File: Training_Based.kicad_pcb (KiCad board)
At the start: 2 copper layers, 210 x 140 mm, 63 parts, among them J1 Conn_01x19, J2 Conn_01x19, J3 Conn_01x19, J4 Conn_01x19, J5 Conn_01x08, J6 Conn_02x02_Row_Letter_Last, J7 Conn_02x02_Row_Letter_Last, J8 Conn_02x02_Row_Letter_Last, K1 FINDER-36.11, K2 FINDER-36.11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

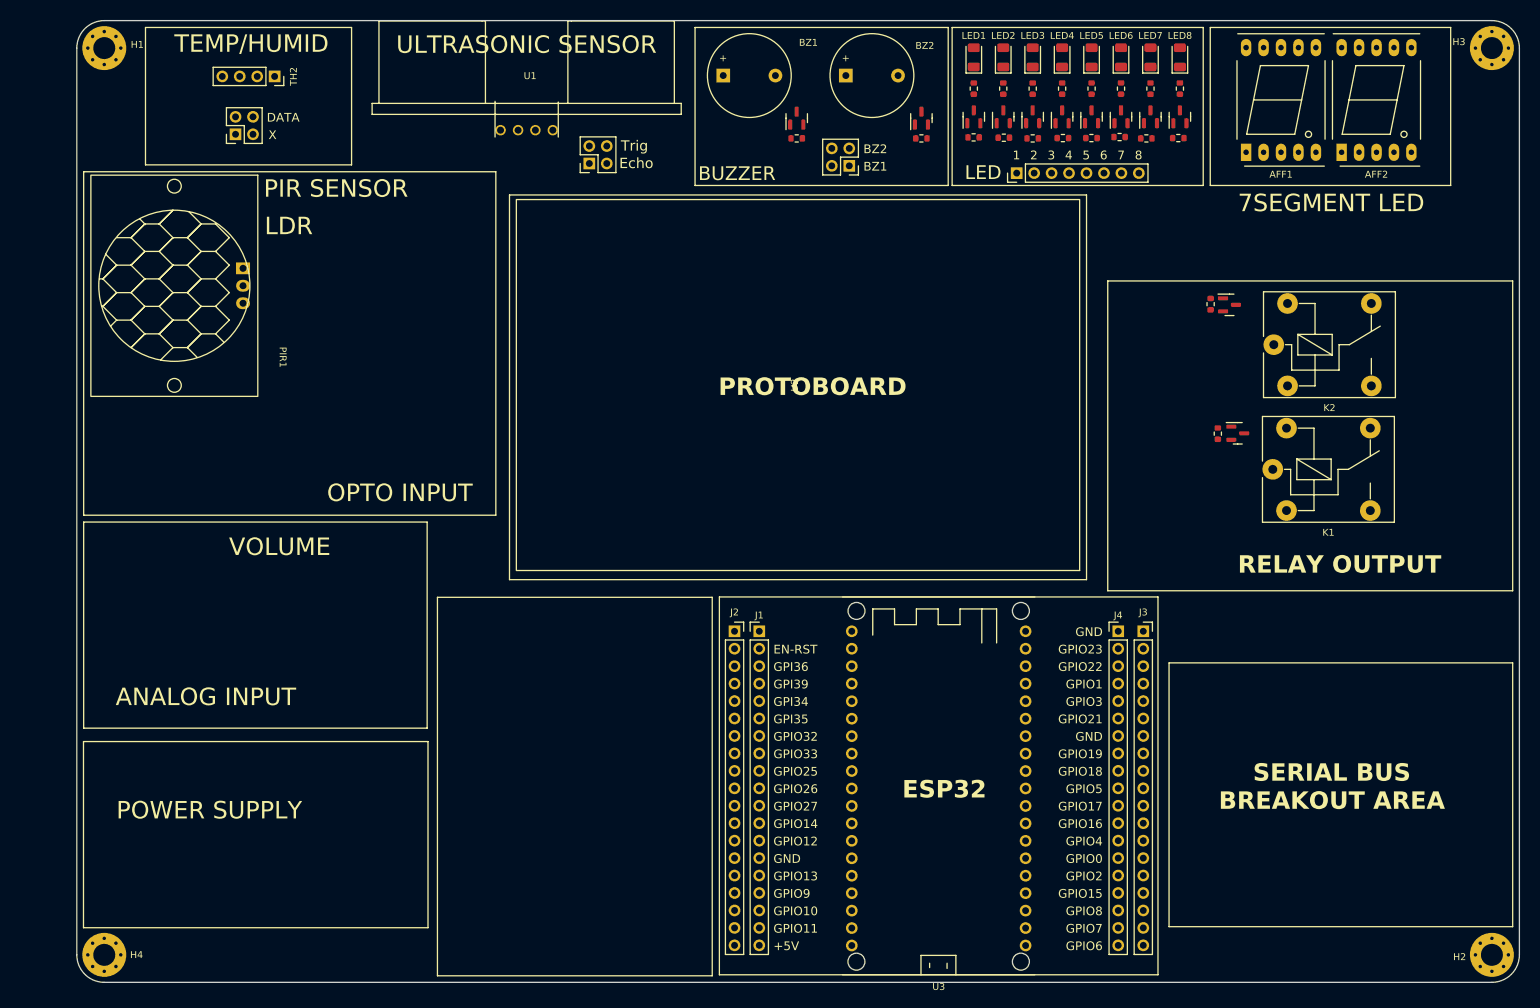
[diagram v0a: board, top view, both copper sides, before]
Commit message: 7 segment and relay
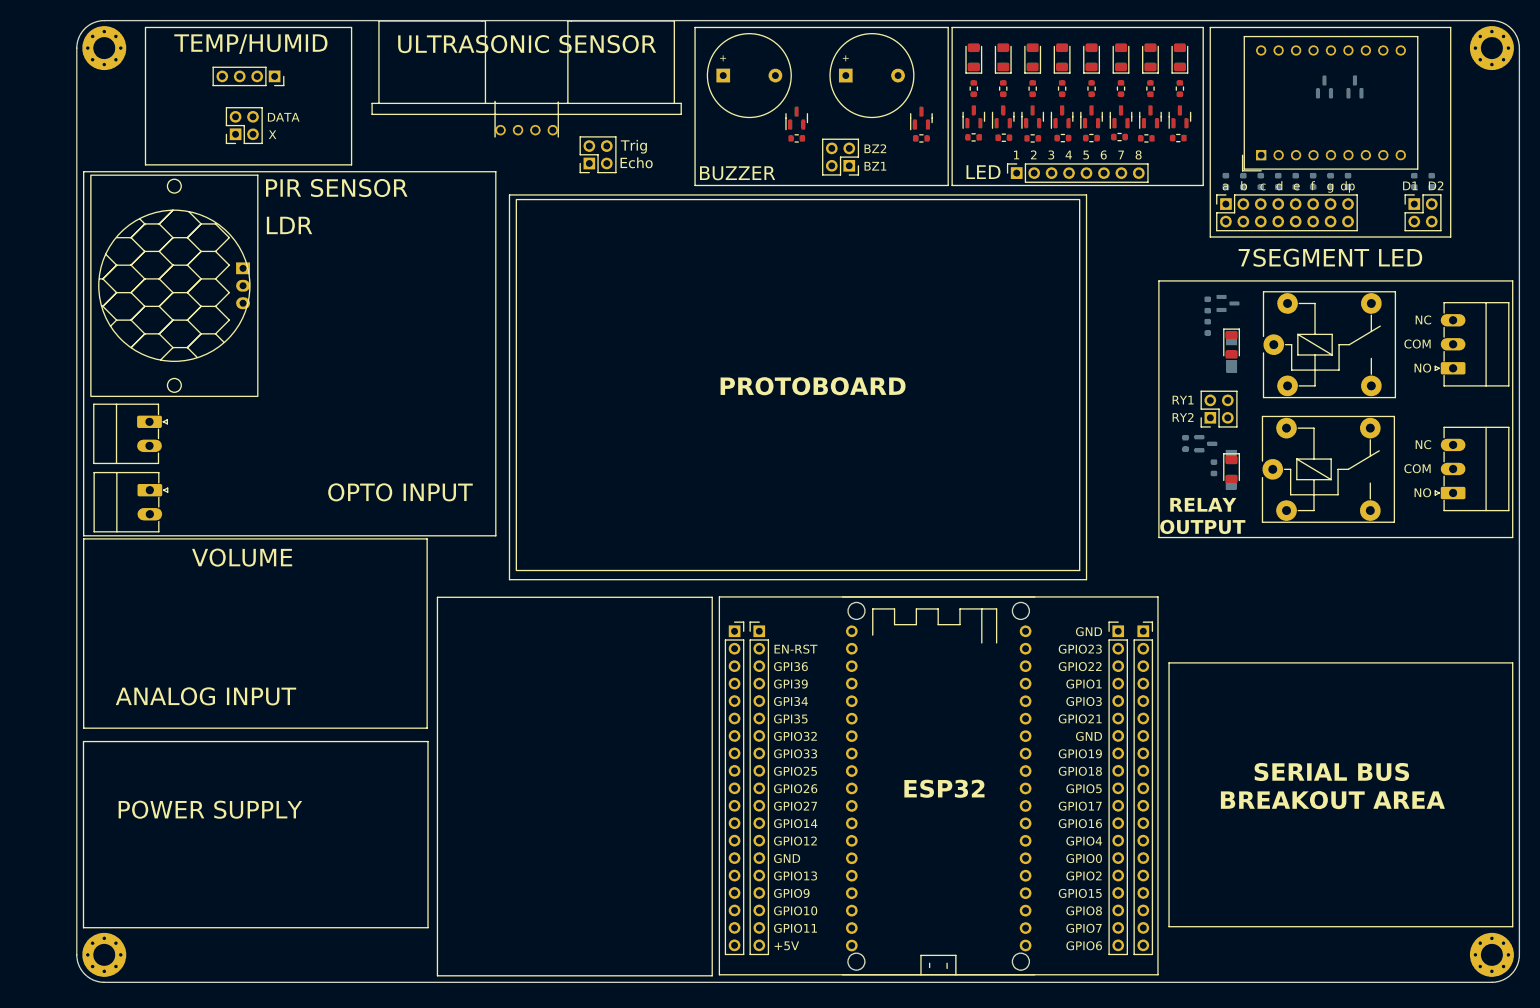
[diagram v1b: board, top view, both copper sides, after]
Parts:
- removed AFF1, AFF2: LTS-6980HR, Display_7Segment:7SegmentLED_LTS6760_LTS6780
- added D1: D, Training_Based:DO-214AC, B.Cu at (188.1, 85.4)
- added D2: D, Training_Based:DO-214AC, B.Cu at (188.1, 68.3)
- added J10: Conn_02x08_Odd_Even, Connector_PinSocket_2.54mm:PinSocket_2x08_P2.54mm_Vertical, F.Cu at (187.3, 46.7)
- added J11: Conn_02x02_Row_Letter_Last, Connector_PinSocket_2.54mm:PinSocket_2x02_P2.54mm_Vertical, F.Cu at (214.7, 46.7)
- added J9: Conn_02x02_Row_Letter_Last, Connector_PinSocket_2.54mm:PinSocket_2x02_P2.54mm_Vertical, F.Cu at (185.0, 77.8)
- added LED10: LED, LED_SMD:LED_1206_3216Metric, F.Cu at (188.1, 67.2)
- added LED9: LED, LED_SMD:LED_1206_3216Metric, F.Cu at (188.1, 85.3)
- added P1: K1, Connector_Phoenix_MC:PhoenixContact_MC_1,5_3-G-3.5_1x03_P3.50mm_Horizontal, F.Cu at (220.3, 88.8)
- added P2: K2, Connector_Phoenix_MC:PhoenixContact_MC_1,5_3-G-3.5_1x03_P3.50mm_Horizontal, F.Cu at (220.3, 70.6)
- added P3: CAN, Connector_Phoenix_MC:PhoenixContact_MC_1,5_2-G-3.5_1x02_P3.50mm_Horizontal, F.Cu at (30.6, 78.4)
- added P4: CAN, Connector_Phoenix_MC:PhoenixContact_MC_1,5_2-G-3.5_1x02_P3.50mm_Horizontal, F.Cu at (30.6, 88.4)
- added Q13: BC817, Package_TO_SOT_SMD:SOT-23, B.Cu at (201.6, 29.6)
- added Q14: BC817, Package_TO_SOT_SMD:SOT-23, B.Cu at (206.1, 29.6)
- added R21: R_Small, Resistor_SMD:R_0603_1608Metric, B.Cu at (214.7, 43.4)
- added R22: R_Small, Resistor_SMD:R_0603_1608Metric, B.Cu at (217.2, 43.4)
- added R23: R_Small, Resistor_SMD:R_0603_1608Metric, B.Cu at (187.3, 43.4)
- added R24: R_Small, Resistor_SMD:R_0603_1608Metric, B.Cu at (189.8, 43.4)
- added R25: R_Small, Resistor_SMD:R_0603_1608Metric, B.Cu at (192.4, 43.4)
- added R26: R_Small, Resistor_SMD:R_0603_1608Metric, B.Cu at (194.9, 43.4)
- added R27: R_Small, Resistor_SMD:R_0603_1608Metric, B.Cu at (197.4, 43.4)
- added R28: R_Small, Resistor_SMD:R_0603_1608Metric, B.Cu at (200.0, 43.4)
- added R29: R_Small, Resistor_SMD:R_0603_1608Metric, B.Cu at (202.5, 43.4)
- added R30: R_Small, Resistor_SMD:R_0603_1608Metric, B.Cu at (205.1, 43.4)
- added R31: R_Small, Resistor_SMD:R_0603_1608Metric, B.Cu at (185.5, 85.1)
- added R32: R_Small, Resistor_SMD:R_0603_1608Metric, B.Cu at (184.6, 64.7)
- added U4: DC56-11SURKWA, Display_7Segment:DA56-11SURKWA, F.Cu at (192.4, 39.6)
- J5: footprint Connector_PinHeader_2.54mm:PinHeader_1x08_P2.54mm_Vertical -> Connector_PinSocket_2.54mm:PinSocket_1x08_P2.54mm_Vertical
- Q11, Q12, R19, R20: moved to B.Cu
- moved R19 4.91 mm to (181.4, 81.5), turned to -90 degrees
- moved Q11 4.89 mm to (184.3, 81.6)
- moved R20 0.44 mm to (184.6, 61.4), turned to -90 degrees
- moved Q12 0.30 mm to (187.6, 61.2)
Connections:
- K1 pad 11: unconnected-(K1-Pad11) -> Net-(P1-Pin_2)
- K1 pad 12: unconnected-(K1-Pad12) -> Net-(P1-Pin_3)
- K1 pad 14: unconnected-(K1-Pad14) -> Net-(P1-Pin_1)
- K2 pad 11: unconnected-(K2-Pad11) -> Net-(P2-Pin_2)
- K2 pad 12: unconnected-(K2-Pad12) -> Net-(P2-Pin_3)
- K2 pad 14: unconnected-(K2-Pad14) -> Net-(P2-Pin_1)
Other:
- board text added: "COM"
- board text added: "D1"
- board text added: "D2"
- board text added: "NC"
- board text added: "NO"
- board text added: "RY1"
- board text added: "RY2"
- board text added: "a"
- board text added: "b"
- board text added: "c"
- board text added: "d"
- board text added: "dp"
- board text added: "e"
- board text added: "f"
- board text added: "g"

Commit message: opto isolator
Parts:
- added J12: Conn_02x02_Row_Letter_Last, Connector_PinSocket_2.54mm:PinSocket_2x02_P2.54mm_Vertical, F.Cu at (197.3, 104.8)
- added J13: SERVO 1, Connector_PinHeader_2.54mm:PinHeader_1x03_P2.54mm_Vertical, F.Cu at (209.9, 98.7)
- added J14: SERVO 2, Connector_PinHeader_2.54mm:PinHeader_1x03_P2.54mm_Vertical, F.Cu at (209.9, 108.3)
- added J15: Conn_02x02_Row_Letter_Last, Connector_PinSocket_2.54mm:PinSocket_2x02_P2.54mm_Vertical, F.Cu at (68.5, 83.9)
- added R33: R_Small, Resistor_THT:R_Axial_DIN0207_L6.3mm_D2.5mm_P10.16mm_Horizontal, F.Cu at (35.8, 81.3)
- added R34: R_Small, Resistor_THT:R_Axial_DIN0207_L6.3mm_D2.5mm_P10.16mm_Horizontal, F.Cu at (35.8, 86.4)
- added R35: R_Small, Resistor_SMD:R_0603_1608Metric, F.Cu at (61.9, 81.3)
- added R36: R_Small, Resistor_SMD:R_0603_1608Metric, F.Cu at (61.9, 86.4)
- added U5: LTV-827, Package_DIP:DIP-8_W7.62mm, F.Cu at (50.6, 81.3)
- P3: value CAN -> OPTO INPUT 1
- P4: value CAN -> OPTO INPUT 2
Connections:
- P3 pad 1: unconnected-(P3-Pin_1) -> Net-(P3-Pin_1)
- P3 pad 2: unconnected-(P3-Pin_2) -> Net-(U5-Pad2)
- P4 pad 1: unconnected-(P4-Pin_1) -> Net-(P4-Pin_1)
- P4 pad 2: unconnected-(P4-Pin_2) -> Net-(P4-Pin_2)
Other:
- board text added: "LEDs"
- board text added: "OPTO IN 1"
- board text added: "OPTO IN 2"
- board text added: "OPTO INPUT 1"
- board text added: "OPTO INPUT 2"
- board text added: "SERVO MOTOR"
- board text added: "SERVO MOTOR 1"
- board text added: "SERVO MOTOR 2"
- board text added: "Servo 1"
- board text added: "Servo 2"
- board text removed: "LED"
- board text removed: "OPTO INPUT"

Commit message: update Optoelectronic parts
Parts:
- added J16: Conn_02x03_Row_Letter_Last, Connector_PinSocket_2.54mm:PinSocket_2x03_P2.54mm_Vertical, F.Cu at (68.5, 70.2)
- added R37: LDR07, OptoDevice:R_LDR_5.1x4.3mm_P3.4mm_Vertical, F.Cu at (55.4, 54.8)
- added R38: R_Small, Resistor_SMD:R_0603_1608Metric, F.Cu at (56.9, 59.4)
- added U6: TSOP382xx, Training_Based:IR_Receiver_TSOP38238, F.Cu at (68.4, 58.8)
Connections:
- PIR1 pad 1: unconnected-(PIR1-GND) -> GND
- PIR1 pad 2: unconnected-(PIR1-DATA) -> /PIR_DATA
- PIR1 pad 3: unconnected-(PIR1-VCC) -> +5V
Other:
- board text added: "IR Rx"
- board text added: "PIR"
- board text removed: "PIR SENSOR"

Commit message: Update Training_Based.kicad_pcb
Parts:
- moved R38 14.2 mm to (61.9, 72.7)
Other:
- board text added: "OPTO Electronic"
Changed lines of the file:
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@@
   )
   (footprint "Resistor_SMD:R_0603_1608Metric" (layer "F.Cu")
-    (at 56.85 59.4)
+    (at 61.9 72.69)
     (descr "Resistor SMD 0603 (1608 Metric), square (rectangular) end terminal, IPC_7351 nominal, (Body size source: IPC-SM-782 page 72, https://www.pcb-3d.com/wordpress/wp-content/uploads/ipc-sm-782a_amendment_1_and_2.pdf), generated with kicad-footprint-generator")
     (tags "resistor")
@@
     (effects (font (size 1.27 1.27) (thickness 0.15)) (justify right bottom))
   )
+  (gr_text "OPTO\nElectronic" (at 56.65 68.1) (layer "F.SilkS")
+    (effects (font (size 2.54 2.54) (thickness 0.2)) (justify bottom))
+  )
   (gr_text "+5V" (at 121.4 155.4656) (layer "F.SilkS")

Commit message: add tact switch and rotary switch
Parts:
- added J17: Conn_02x07_Odd_Even, Connector_PinSocket_2.54mm:PinSocket_2x05_P2.54mm_Vertical, F.Cu at (100.0, 114.2)
- added LED11: LED, LED_SMD:LED_1206_3216Metric, F.Cu at (101.7, 140.6)
- added LED12: LED, LED_SMD:LED_1206_3216Metric, F.Cu at (81.7, 140.6)
- added R39: R_Small, Resistor_SMD:R_0603_1608Metric, F.Cu at (103.4, 143.0)
- added R40: R_Small, Resistor_SMD:R_0603_1608Metric, F.Cu at (100.0, 143.0)
- added R41: R_Small, Resistor_SMD:R_0603_1608Metric, F.Cu at (83.4, 143.0)
- added R42: R_Small, Resistor_SMD:R_0603_1608Metric, F.Cu at (80.0, 143.0)
- added SW1: RotaryEncoder_Switch, Rotary_Encoder:RotaryEncoder_Alps_EC11E-Switch_Vertical_H20mm, F.Cu at (80.0, 125.0)
- added SW2: SW_Push, Button_Switch_THT:SW_PUSH_6mm_H5mm, F.Cu at (105.0, 150.0)
- added SW3: SW_Push, Button_Switch_THT:SW_PUSH_6mm_H5mm, F.Cu at (85.0, 150.0)
- U6: footprint Training_Based:IR_Receiver_TSOP38238 -> OptoDevice:Vishay_MINICAST-3Pin
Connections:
- U4 pad 10: unconnected-(U4-DIG2_B) -> /S_B
- U4 pad 11: unconnected-(U4-DIG2_A) -> /S_A
- U4 pad 12: unconnected-(U4-DIG2_F) -> /S_F
- U4 pad 5: unconnected-(U4-DIG2_E) -> /S_E
- U4 pad 6: unconnected-(U4-DIG2_D) -> /S_D
- U4 pad 7: unconnected-(U4-DIG2_G) -> /S_G
- U4 pad 8: unconnected-(U4-DIG2_C) -> /S_C
- U4 pad 9: unconnected-(U4-DP2) -> /S_DP
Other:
- board text added: "PUSH BT1"
- board text added: "PUSH BT2"
- board text added: "Rotary A"
- board text added: "Rotary B"
- board text added: "Rotary S1"

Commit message: finish layout
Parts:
- added C1: 22uF/6.3V, Capacitor_SMD:C_0603_1608Metric, F.Cu at (35.9, 145.7)
- added C2: 1nF/50V, Capacitor_SMD:C_0603_1608Metric, F.Cu at (42.0, 150.2)
- added C3: 100uF/35V, Capacitor_SMD:CP_Elec_6.3x7.7, F.Cu at (44.1, 139.2)
- added C4: 100nF/50V, Capacitor_SMD:C_0603_1608Metric, F.Cu at (46.7, 145.8)
- added C5: 100uF/35V, Capacitor_SMD:CP_Elec_6.3x7.7, F.Cu at (44.1, 131.7)
- added F1: 3.00A, Fuse:Fuse_1210_3225Metric, F.Cu at (35.1, 140.8)
- added J18: Conn_02x02_Row_Letter_Last, Connector_PinSocket_2.54mm:PinSocket_2x02_P2.54mm_Vertical, F.Cu at (52.0, 106.5)
- added J19: USB_B_Mini, Connector_USB:USB_Mini-B_Lumberg_2486_01_Horizontal, F.Cu at (27.5, 144.8)
- added J20: Conn_02x07_Odd_Even, Connector_PinSocket_2.54mm:PinSocket_2x05_P2.54mm_Vertical, F.Cu at (52.0, 130.6)
- added J21: Conn_02x07_Odd_Even, Connector_PinSocket_2.54mm:PinSocket_2x05_P2.54mm_Vertical, F.Cu at (52.0, 138.2)
- added J22: Conn_02x07_Odd_Even, Connector_PinSocket_2.54mm:PinSocket_2x05_P2.54mm_Vertical, F.Cu at (52.0, 145.9)
- added J23: Conn_01x08, Connector_PinSocket_2.54mm:PinSocket_1x08_P2.54mm_Vertical, F.Cu at (195.1, 119.4)
- added J24: Conn_01x08, Connector_PinSocket_2.54mm:PinSocket_1x08_P2.54mm_Vertical, F.Cu at (195.1, 149.4)
- added L1: 2.2uH/1.5A, Inductor_SMD:L_Neosid_SMS-ME3015, F.Cu at (43.6, 145.8)
- added P5: Voltage Input, Connector_Phoenix_MC:PhoenixContact_MC_1,5_2-G-3.5_1x02_P3.50mm_Horizontal, F.Cu at (30.6, 119.0)
- added R43: R_Small, Resistor_THT:R_Axial_DIN0207_L6.3mm_D2.5mm_P10.16mm_Horizontal, F.Cu at (49.0, 119.0)
- added R44: R_Small, Resistor_THT:R_Axial_DIN0207_L6.3mm_D2.5mm_P10.16mm_Horizontal, F.Cu at (38.9, 122.5)
- added R46: 220k, Resistor_SMD:R_0603_1608Metric, F.Cu at (42.0, 148.6)
- added R47: 49.9k/1%, Resistor_SMD:R_0603_1608Metric, F.Cu at (38.9, 148.6)
- added RV1: R_Potentiometer, Potentiometer_THT:Potentiometer_Alps_RK163_Single_Horizontal, F.Cu at (29.8, 99.8)
- added U7: SY8089AAAC(SOT23-5), Package_TO_SOT_SMD:SOT-23-5, F.Cu at (39.4, 145.8)
- moved J17 2.36 mm to (99.8, 116.5)
- moved SW1 2.36 mm to (79.8, 127.3)
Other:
- board text added: "+3.3V"
- board text added: "+5.0V"
- board text added: "V+"
- board text added: "V-"

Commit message: Update Training_Based.kicad_pcb
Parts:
- added LED13: RED 1206, LED_SMD:LED_1206_3216Metric, F.Cu at (35.2, 136.9)
- added R45: 470, Resistor_SMD:R_0603_1608Metric, F.Cu at (30.6, 136.9)
- BZ1: value Buzzer -> Buzzer (IN)
- BZ2: value Buzzer -> Buzzer (EX)
- D1, D2: value D -> M7
- J1: value Conn_01x19 -> ESP32_LEFT_A
- J10: value Conn_02x08_Odd_Even -> 7 Segment Digit
- J11: value Conn_02x02_Row_Letter_Last -> 7 Segment Common
- J12: value Conn_02x02_Row_Letter_Last -> SERVO MOTOR
- J15: value Conn_02x02_Row_Letter_Last -> OPTO ISOLATOR
- J16: value Conn_02x03_Row_Letter_Last -> OPTO
- J17: value Conn_02x07_Odd_Even -> SWITCH
- J18: value Conn_02x02_Row_Letter_Last -> Analog Input
- J2: value Conn_01x19 -> ESP32_LEFT_B
- J20: value Conn_02x07_Odd_Even -> +5V
- J21: value Conn_02x07_Odd_Even -> +3.3V
- J22: value Conn_02x07_Odd_Even -> GND
- J3: value Conn_01x19 -> ESP32_RIGHT_A
- J4: value Conn_01x19 -> ESP32_RIGHT_B
- J5: value Conn_01x08 -> LED x8
- J6: value Conn_02x02_Row_Letter_Last -> TEMP-HUMID
- J7: value Conn_02x02_Row_Letter_Last -> Ultrasonic
- J8: value Conn_02x02_Row_Letter_Last -> Buzzer
- J9: value Conn_02x02_Row_Letter_Last -> RELAY
- LED1, LED10, LED11, LED12, LED2, LED3, LED4, LED5, LED6, LED7, LED8, LED9: value LED -> RED 1206
- R1, R10, R12, R14, R16, R23, R24, R25, R26, R27, R28, R29, R30, R31, R32, R39, R4, R42, R6, R8: value R_Small -> 470
- R11, R13, R15, R17, R18, R19, R2, R20, R21, R22, R3, R38, R40, R41, R5, R7, R9: value R_Small -> 10k
- R33, R34: value R_Small -> 1k
- R35, R36: value R_Small -> 47k
- RV1: value R_Potentiometer -> 50kB
- moved R13 0.61 mm to (176.3, 37.0)
- moved R15 0.25 mm to (180.6, 37.0)
- moved R11 0.21 mm to (172.0, 37.0)
- moved R7 0.15 mm to (163.4, 37.0)
- moved R5 0.15 mm to (159.2, 37.0)
- moved R9 0.10 mm to (167.7, 37.0)
- moved R3 0.10 mm to (154.9, 37.0)
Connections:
- C1 pad 1: /IN -> +5V
- F1 pad 1: /IN -> +5V
- U7 pad 1: /IN -> +5V
- U7 pad 4: /IN -> +5V

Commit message: Update Training_Based.kicad_pcb
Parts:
- moved R39 3.40 mm to (100.0, 143.0), turned to 180 degrees
- moved R40 3.40 mm to (103.4, 143.0), turned to 0 degrees
- moved R35 0.83 mm to (61.9, 82.2), turned to -90 degrees
- moved R36 0.83 mm to (61.9, 85.6), turned to 90 degrees
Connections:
- J1 pad 1: +3.3V -> /+3.3V_ESP
- J2 pad 1: +3.3V -> /+3.3V_ESP
- U3 pad 1: +3.3V -> /+3.3V_ESP
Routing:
- net +5V: track 0.00 -> 794.2 mm
- net +3.3V: track 0.00 -> 282.9 mm, vias 0 -> 3
- net /S_F: track 0.00 -> 46.2 mm, vias 0 -> 1
- net /S2_PB: track 0.00 -> 41.3 mm
- net /S_B: track 0.00 -> 38.3 mm
- net /S_A: track 0.00 -> 38.1 mm
- net /S1_PB: track 0.00 -> 38.0 mm
- net GND: track 0.00 -> 36.7 mm, vias 0 -> 7
- net /PIR_DATA: track 0.00 -> 33.7 mm
- net /S_G: track 0.00 -> 28.6 mm
- net Net-(P1-Pin_2): track 0.00 -> 26.2 mm
- net Net-(P2-Pin_2): track 0.00 -> 26.0 mm
- net /LDR_OUTPUT: track 0.00 -> 25.4 mm
- net /S_DP: track 0.00 -> 25.2 mm
- net /A_Rotary: track 0.00 -> 24.3 mm
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- added copper zone on F.Cu, net GND
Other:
- board text added: "ESP_3.3V"
